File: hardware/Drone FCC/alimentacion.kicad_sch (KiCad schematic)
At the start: 20 parts, among them J28 PM02 PixHawk, Q1 Q_PMOS_GSD, U6 ZLDO1117QG33TA

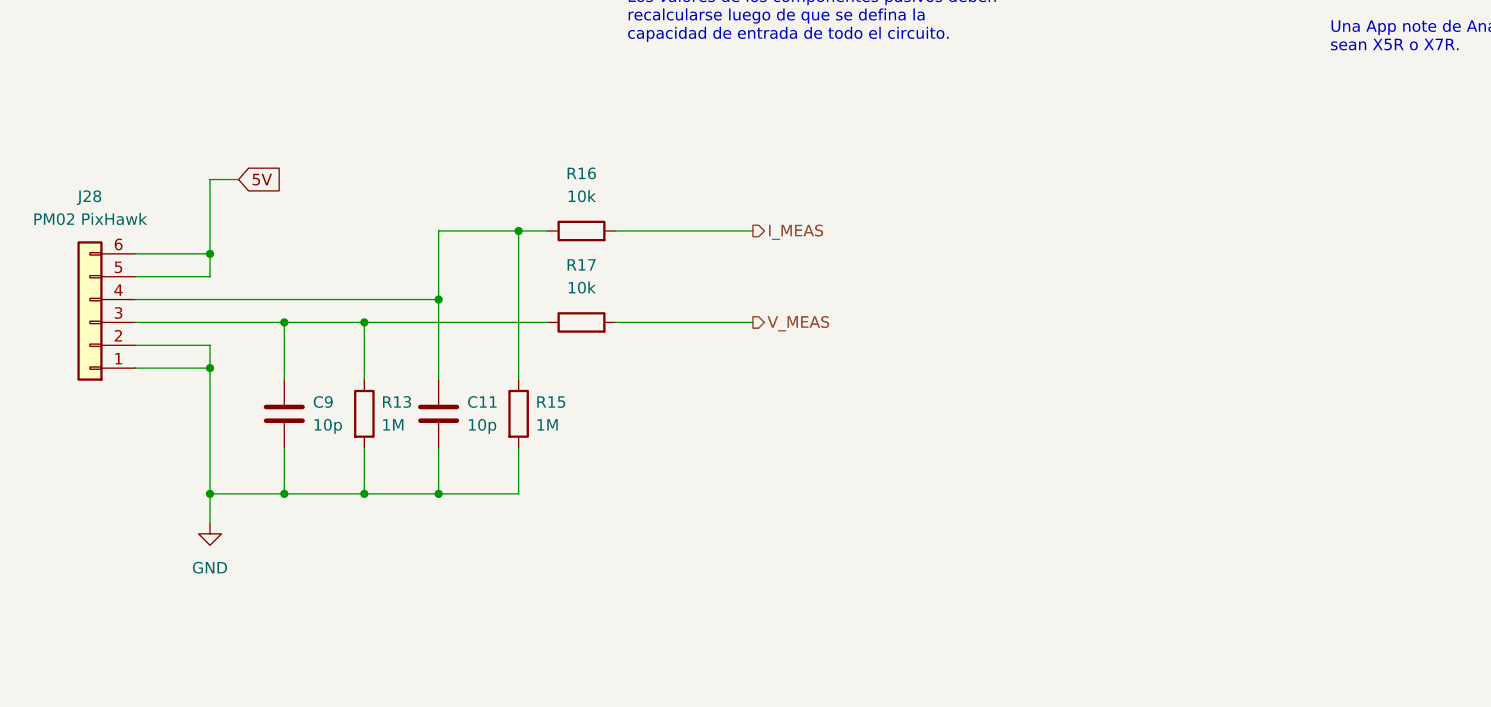
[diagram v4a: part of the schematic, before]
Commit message: add external communication connectors
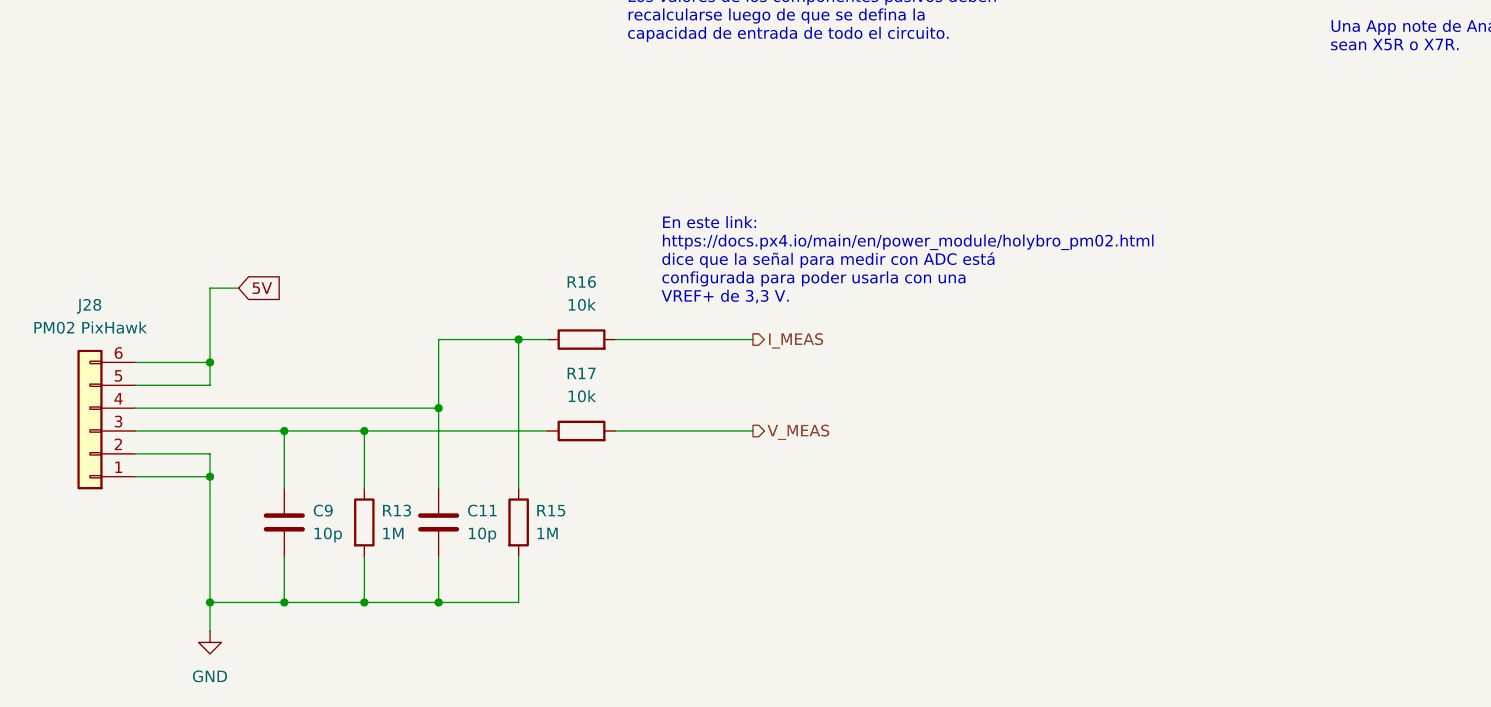
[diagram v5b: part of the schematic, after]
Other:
- note added: "En este link: https://docs.px4.io/main/en/power_module/holybro_pm02.html dice que la señal para medir con ADC está configurada para poder usarla con una VREF+ de 3,3 V."
- moved on the sheet: C11, C9, J28, R13, R15, R16, R17

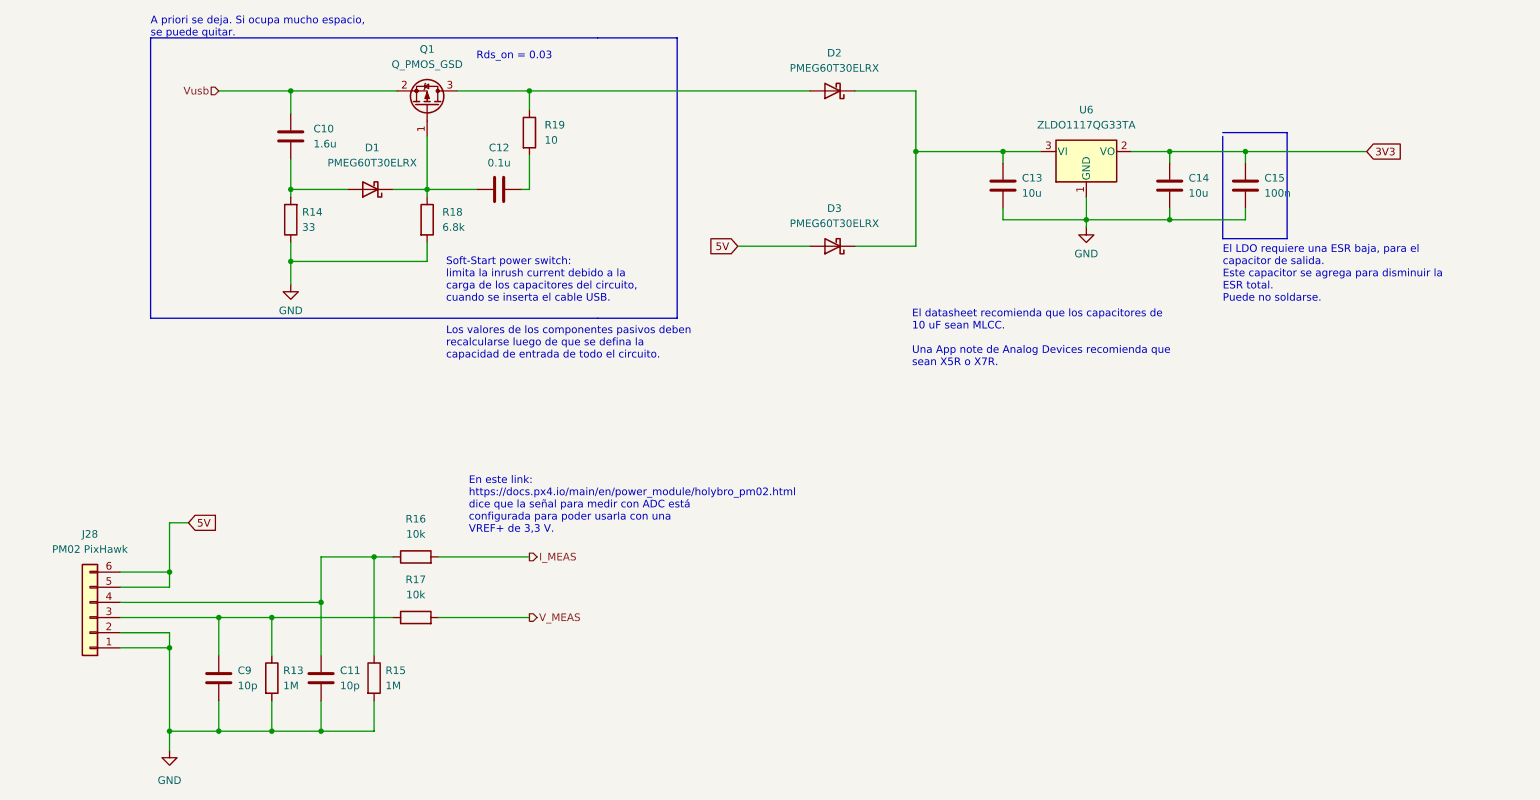
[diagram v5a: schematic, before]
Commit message: re enumeration of components
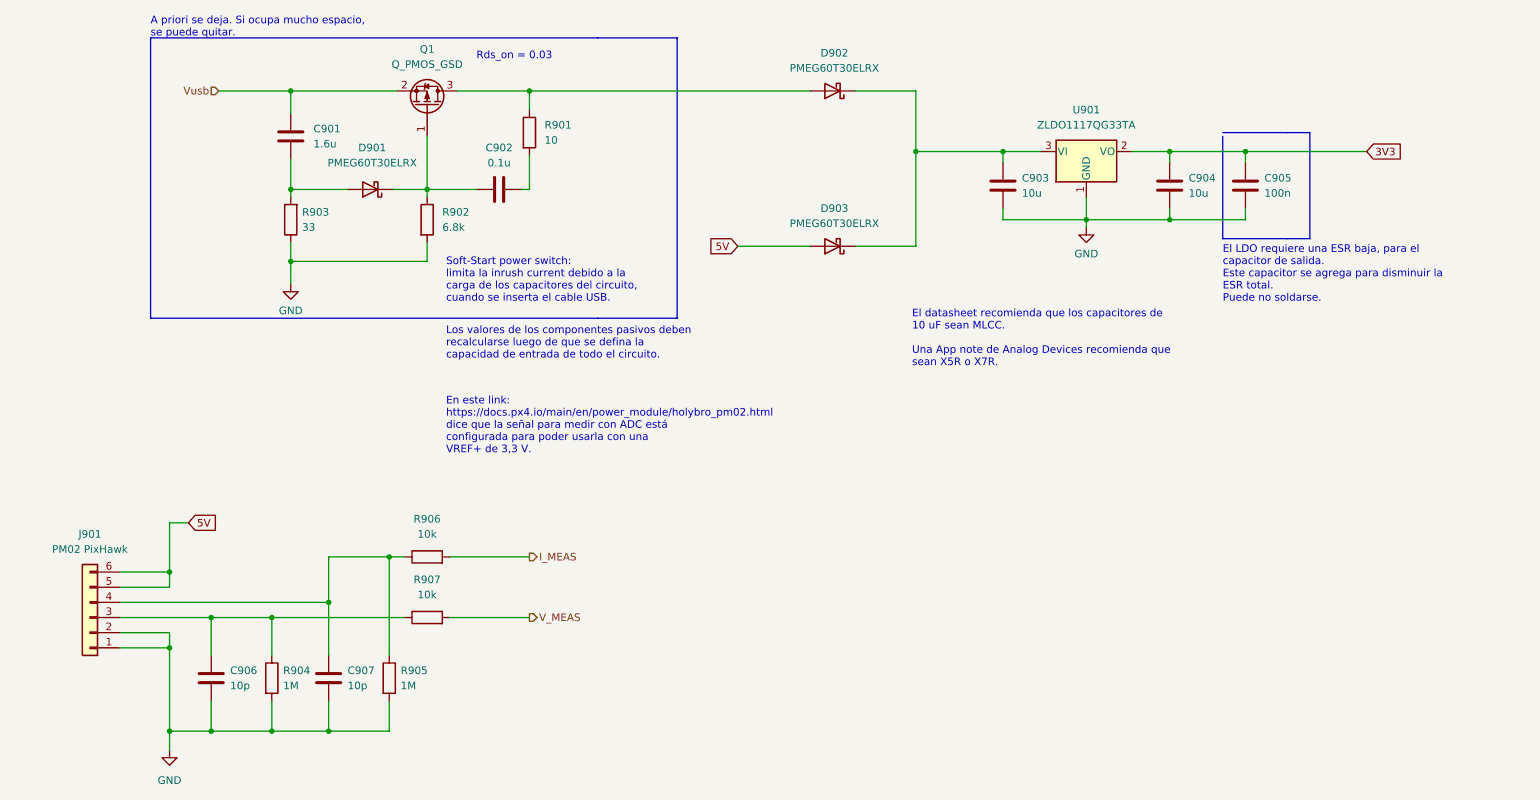
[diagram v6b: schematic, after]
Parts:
- renumbered C10 to C901, C12 to C902, C13 to C903, C14 to C904, C15 to C905, C9 to C906, C11 to C907, D1 to D901, D2 to D902, D3 to D903, J28 to J901, R19 to R901, R18 to R902, R14 to R903, R13 to R904, R15 to R905, R16 to R906, R17 to R907, U6 to U901
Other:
- moved on the sheet: C906, C907, R905, R906, R907

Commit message: start routing
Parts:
- removed J901: PM02 PixHawk, Connector_Hirose:Hirose_DF13C_CL535-0406-3-51_1x06-1MP_P1.25mm_Vertical, symbol Connector_Generic:Conn_01x06
- added J901: PM02 PixHawk, DF13C-6P-1.25V(51):HIROSE_DF13C-6P-1.25V(51), symbol DF13C-69-1.25v(51):DF13C-6P-1.25V(51)
- C901, C902, C905: footprint (none) -> Capacitor_SMD:C_0603_1608Metric_Pad1.08x0.95mm_HandSolder
- C903, C904: footprint (none) -> Capacitor_SMD:C_0805_2012Metric_Pad1.18x1.45mm_HandSolder
- C906, C907: value 10p -> 100p; footprint (none) -> Capacitor_SMD:C_0402_1005Metric_Pad0.74x0.62mm_HandSolder
- D901, D902, D903: footprint (none) -> PMEG60T30ELRX:SODFL3517X110N
- Q901: renamed from Q1; footprint (none) -> Package_TO_SOT_SMD:SOT-23
- R901, R902, R903: footprint (none) -> Resistor_SMD:R_0603_1608Metric_Pad0.98x0.95mm_HandSolder
- R904, R905, R906, R907: footprint (none) -> Resistor_SMD:R_0402_1005Metric_Pad0.72x0.64mm_HandSolder
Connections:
- net 5V: now also J901.1, J901.2
- net GND: now also J901.5, J901.6, J901.S1 (SHIELD), J901.S2 (SHIELD)
- net at C906.1, R904.1, R907.1: now also J901.4
- net at C907.1, R905.1, R906.1: now also J901.3

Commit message: continued preliminar routing
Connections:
- net Vusb: now also D902.2 (A)
- net at Q901.3 (D), R901.1: no longer D902.2 (A)
- net 5Vin: now reaches C903.1, D902.1 (K), D903.1 (K), U901.3 (VI)
